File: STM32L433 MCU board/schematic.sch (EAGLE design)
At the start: 15 parts, among them T1 2N2222, U1 STM32L433CCT6, Y1 ECS-160-8-30B-CKM

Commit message: Add files via upload
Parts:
- removed R1: 1k, SparkFun-Resistors:1KOHM-0603-1/10W-1%
- removed R2: 220, SparkFun-Resistors:220OHM-0603-1/10W-1%
- removed R3: 44.2k, SparkFun-Resistors:1KOHM-0603-1/10W-1%
- removed R4: 16k, SparkFun-Resistors:1KOHM-0603-1/10W-1%
- removed R5, R6: 10k, SparkFun-Resistors:1KOHM-0603-1/10W-1%
- removed Y1: ECS-160-8-30B-CKM, ECS-160-8-30B-CKM:ECS-160-8-30B-CKM
- added R10: 1k, adafruit:R-US_R0805
- added R11, R12: 10k, adafruit:R-US_R0805
- added R7: 44.2k, adafruit:R-US_R0805
- added R8: 16k, adafruit:R-US_R0805
- added R9: 220, adafruit:R-US_R0805
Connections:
- removed net N$7: Y1.GND
- new net SD_CS: U$1.CS, U1.PB4
- net 3.3V: now also R11.1, R12.1; no longer R5.2, R6.2
- net BUZZ: now also R9.1, U1.PA8; no longer R2.1
- net CS1: now also U1.PB5
- net CS2: now also U1.PB6
- net CS3: now also U1.PB7
- net CS4: now also U1.PB8
- net CS5: now also U1.PB9
- net GND: now also R8.1; no longer R4.1
- net IGN_CHK1: now also U1.PA1, U1.PA2
- net IGN_CHK2: now also U1.PA3
- net IGN_CHK3: now also U1.PA4
- net LIPO: now also R10.2, R7.2; no longer R1.2, R3.2
- net N$2: now also R9.2; no longer R2.2
- net N$3: now also R10.1; no longer R1.1
- net N$4: now also R11.2; no longer R6.1
- net N$5: now also R7.1, R8.2, U1.PA0; no longer R3.1, R4.2
- net N$6: now also R12.2; no longer R5.1
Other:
- note added: "To-do: find and implement oscillators add bypass capacitors add LEDs"
- note removed: "Need to add chip select Just needs to be a regular digital pin"
- note removed: "To-do: wire buzzer digital pin chip select for microSD card wire lipo voltage analog pin into something wire continuity checking lines into ADC input find and implement oscillators add bypass capacitors add LEDs"
- moved on the sheet: JP3

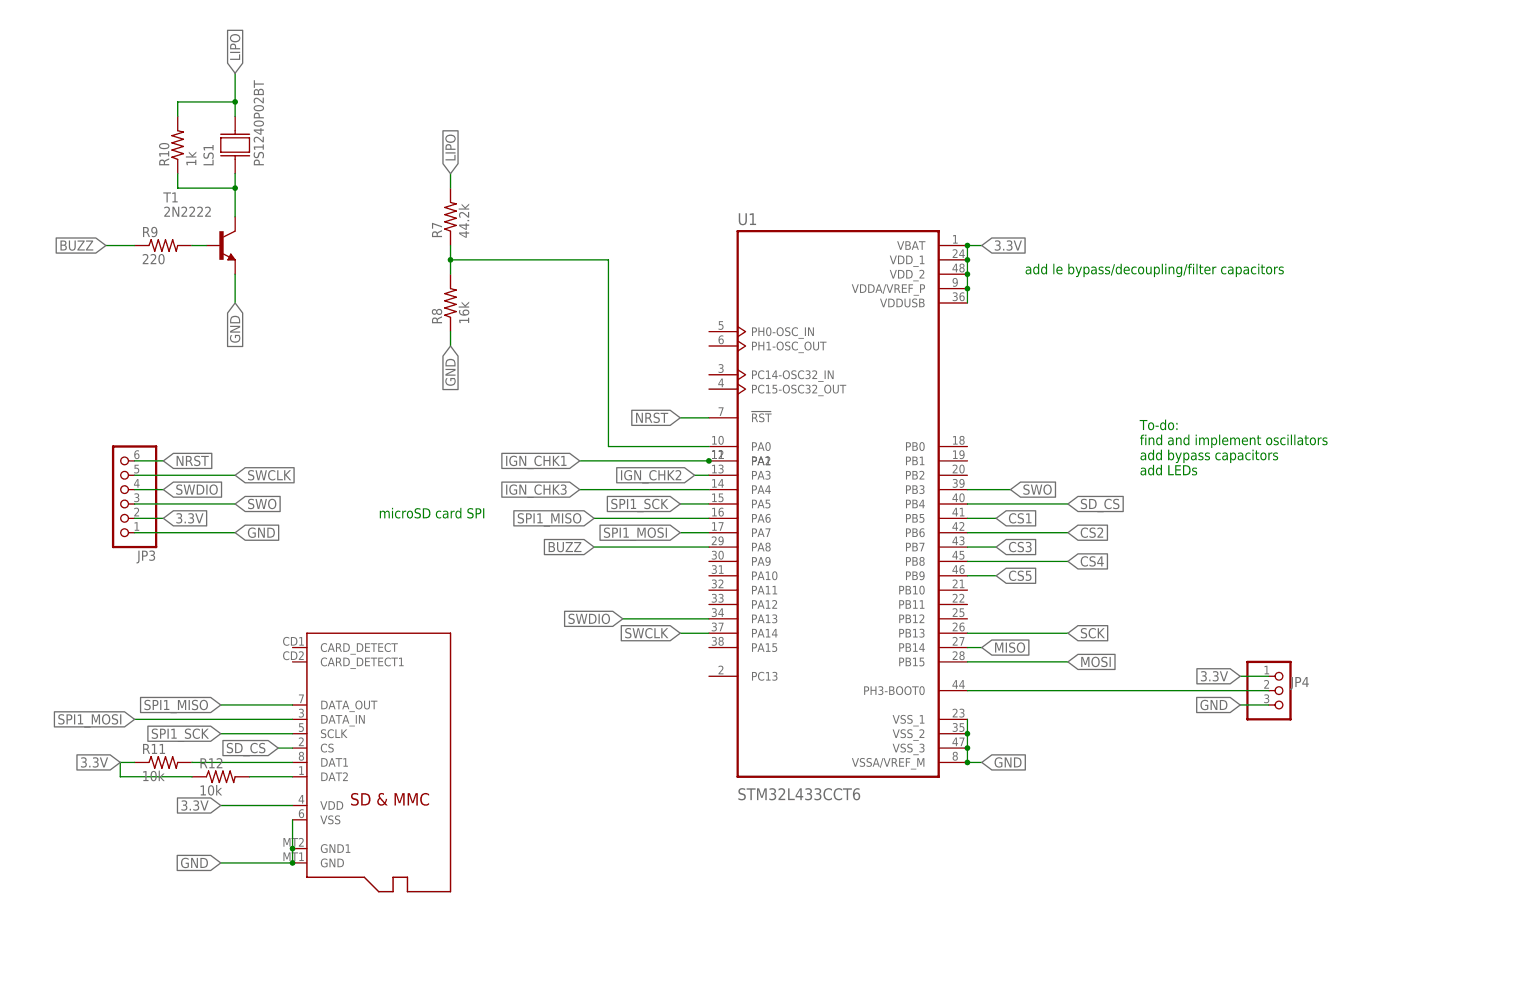
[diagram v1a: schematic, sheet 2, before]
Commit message: Finished MCU board routing
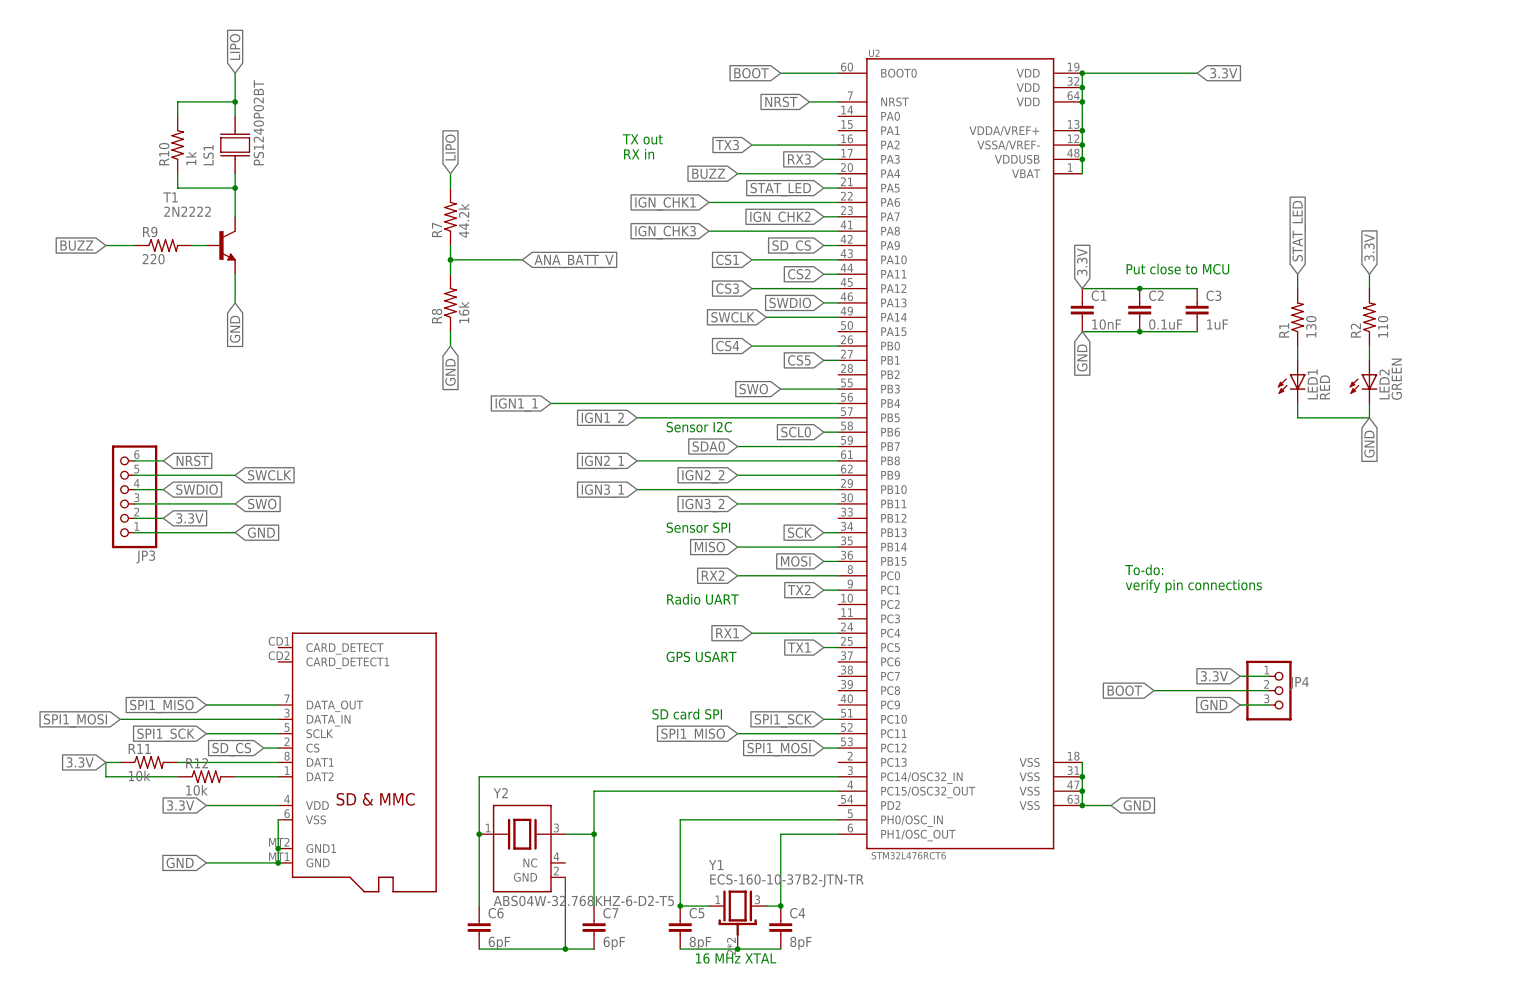
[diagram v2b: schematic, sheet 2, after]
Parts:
- removed U1: STM32L433CCT6, STM32L433CCT6:STM32L433CCT6
- added C1: 10nF, rcl:C-EUC0805
- added C2: 0.1uF, rcl:C-EUC0805
- added C3: 1uF, rcl:C-EUC0805
- added C4, C5: 8pF, rcl:C-EUC0805
- added C6, C7: 6pF, rcl:C-EUC0805
- added LED1: RED, adafruit:LEDCHIPLED_0805
- added LED2: GREEN, adafruit:LEDCHIPLED_0805
- added R1: 130, adafruit:R-US_R0805
- added R2: 110, adafruit:R-US_R0805
- added U2: STM32L476RCT6, STM32L476RCT6:STM32L476RCT6
- added Y1: ECS-160-10-37B2-JTN-TR, ECS-160-10-37B2-JTN-TR:ECS-160-10-37B2-JTN-TR
- added Y2: ABS04W-32.768KHZ-6-D2-T5, ABS04W-32.768KHZ-6-D2-T5:ABS04W-32.768KHZ-6-D2-T5
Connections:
- net 5V renamed 3V3.2
- new net ANA_BATT_V: R7.1, R8.2
- new net BOOT: JP4.2, U2.BOOT0
- new net N$10: C6.2, C7.2, Y2.GND
- new net N$11: C7.1, U2.PC15/OSC32_OUT, Y2.2
- new net N$12: C6.1, U2.PC14/OSC32_IN, Y2.1
- new net N$7: LED1.A, R1.1
- new net N$8: LED2.A, R2.1
- new net N$9: C4.2, C5.2, Y1.GND
- new net STAT_LED: R1.2, U2.PA5
- net 3.3V: now also C1.1, C2.1, C3.1, R2.2, U2.VBAT, U2.VDD@1, U2.VDD@2, U2.VDD@3, U2.VDDA/VREF+, U2.VDDUSB, U2.VSSA/VREF-; no longer U1.VBAT, U1.VDDA/VREF_P, U1.VDDUSB, U1.VDD_1, U1.VDD_2
- net BUZZ: now also U2.PA4; no longer U1.PA8
- net CS1: now also U2.PA10; no longer U1.PB5
- net CS2: now also U2.PA11; no longer U1.PB6
- net CS3: now also U2.PA12; no longer U1.PB7
- net CS4: now also U2.PB0; no longer U1.PB8
- net CS5: now also U2.PB1; no longer U1.PB9
- net GND: now also C1.2, C2.2, C3.2, LED1.C, LED2.C, U2.VSS@1, U2.VSS@2, U2.VSS@3, U2.VSS@4; no longer U1.VSSA/VREF_M, U1.VSS_1, U1.VSS_2, U1.VSS_3
- net IGN1_1: now also U2.PB4
- net IGN1_2: now also U2.PB5
- net IGN2_1: now also U2.PB8
- net IGN2_2: now also U2.PB9
- net IGN3_1: now also U2.PB10
- net IGN3_2: now also U2.PB11
- net IGN_CHK1: now also U2.PA6; no longer U1.PA1, U1.PA2
- net IGN_CHK2: now also U2.PA7; no longer U1.PA3
- net IGN_CHK3: now also U2.PA8; no longer U1.PA4
- net MISO: now also U2.PB14; no longer U1.PB14
- net MOSI: now also U2.PB15; no longer U1.PB15
- net N$1: now also C5.1, U2.PH0/OSC_IN, Y1.1; no longer JP4.2, U1.PH3-BOOT0
- net N$5: now also C4.1, U2.PH1/OSC_OUT, Y1.3; no longer R7.1, R8.2, U1.PA0
- net NRST: now also U2.NRST; no longer U1.!RST
- net RX1: now also U2.PC4
- net RX2: now also U2.PC0
- net RX3: now also U2.PA3
- net SCK: now also U2.PB13; no longer U1.PB13
- net SCL0: now also U2.PB6
- net SDA0: now also U2.PB7
- net SD_CS: now also U2.PA9; no longer U1.PB4
- net SPI1_MISO: now also U2.PC11; no longer U1.PA6
- net SPI1_MOSI: now also U2.PC12; no longer U1.PA7
- net SPI1_SCK: now also U2.PC10; no longer U1.PA5
- net SWCLK: now also U2.PA14; no longer U1.PA14
- net SWDIO: now also U2.PA13; no longer U1.PA13
- net SWO: now also U2.PB3; no longer U1.PB3
- net TX1: now also U2.PC5
- net TX2: now also U2.PC1
- net TX3: now also U2.PA2
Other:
- note added: "16 MHz XTAL"
- note added: "GPS USART"
- note added: "Put close to MCU"
- note added: "Radio UART"
- note added: "SD card SPI"
- note added: "Sensor I2C"
- note added: "Sensor SPI"
- note added: "TX out RX in"
- note added: "To-do: verify pin connections"
- note removed: "To-do: find and implement oscillators add bypass capacitors add LEDs"
- note removed: "add le bypass/decoupling/filter capacitors"
- note removed: "microSD card SPI"
- moved on the sheet: R11, R12
